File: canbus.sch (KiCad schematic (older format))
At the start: 14 parts, among them U6 ISO1050DUB

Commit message: Update according to comments
Also add missing connectors and update the fuses
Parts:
- removed FB?: GZ2012D601TF, symbol Device:Ferrite_Bead
- added C601: 10nF/50V, symbol Device:C
- added J602: Conn_02x02_Counter_Clockwise, symbol Connector_Generic:Conn_02x02_Counter_Clockwise
- added U601: RCLAMP0524P-N, symbol SH-ESP32:RCLAMP0524P-N
- F601: renamed from F?; value SMD1206P010TF -> FSMD012-1206-R; LCSC C20981 -> (none)
- gave numbers to parts that had none: 7
- renumbered C10 to C602, C9 to C604, JP1 to JP601, R11 to R601, U6 to U602
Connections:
- net labels added: Vin
- wire segments 46 -> 65
- no-connect marks 0 -> 4
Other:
- note added: "Optional termination\nresistance for the bus"
- note added: "This jumper can be bridged to\npower the whole device from\nCAN bus."
- moved on the sheet: F601, FB601, JP601, R601

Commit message: Rough PCB layout
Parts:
- removed J601: Screw_Terminal_01x05, symbol Connector:Screw_Terminal_01x05
- removed J602: Conn_02x02_Counter_Clockwise, symbol Connector_Generic:Conn_02x02_Counter_Clockwise
- added J601: Conn_01x04, Connector_Phoenix_MC:PhoenixContact_MCV_1,5_4-G-3.81_1x04_P3.81mm_Vertical, symbol Connector_Generic:Conn_01x04
- C601: footprint (none) -> Capacitor_SMD:C_0603_1608Metric
- C602, C604: footprint Capacitor_SMD:C_0603_1608Metric -> Capacitor_SMD:C_0402_1005Metric
- C603: footprint Capacitor_SMD:C_1206_3216Metric -> Capacitor_SMD:C_0805_2012Metric
- FB601: footprint (none) -> Inductor_SMD:L_0805_2012Metric
- U601: footprint (none) -> Package_DFN_QFN:Diodes_UDFN-10_1.0x2.5mm_P0.5mm
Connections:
- net labels added: +3.3V
- net labels removed: 3.3V, CAN_SHIELD, GNDPWR, Vin
- wire segments 65 -> 57
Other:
- note added: "NMEA 2000"
- note removed: "CAN bus"
- note removed: "This jumper can be bridged to\npower the whole device from\nCAN bus."
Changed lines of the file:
@@
 	6550 4000 6350 4000
-Wire Wire Line
-	6550 3150 6550 3350
 Wire Wire Line
 	6450 4300 6350 4300
@@
 F 0 "C604" H 6500 3650 50  0000 L CNN
 F 1 "100nF" H 6450 3550 50  0000 L CNN
-F 2 "Capacitor_SMD:C_0603_1608Metric" H 6838 3450 50  0001 C CNN
+F 2 "Capacitor_SMD:C_0402_1005Metric" H 6838 3450 50  0001 C CNN
 F 3 "~" H 6800 3600 50  0001 C CNN
 F 4 "C14663" H 6800 3600 50  0001 C CNN "LCSC"
@@
 Wire Wire Line
 	6800 3350 6550 3350
-Connection ~ 6550 3350
 Wire Wire Line
 	6550 3350 6550 4000
@@
 F 0 "C602" H 5015 4296 50  0000 L CNN
 F 1 "100nF" H 5015 4205 50  0000 L CNN
-F 2 "Capacitor_SMD:C_0603_1608Metric" H 4938 4100 50  0001 C CNN
+F 2 "Capacitor_SMD:C_0402_1005Metric" H 4938 4100 50  0001 C CNN
 F 3 "~" H 4900 4250 50  0001 C CNN
 F 4 "C14663" H 4900 4250 50  0001 C CNN "LCSC"
@@
 F 0 "FB601" V 4176 1450 50  0000 C CNN
 F 1 "GZ2012D601TF" V 4267 1450 50  0000 C CNN
-F 2 "" V 4380 1450 50  0001 C CNN
+F 2 "Inductor_SMD:L_0805_2012Metric" V 4380 1450 50  0001 C CNN
 F 3 "~" H 4450 1450 50  0001 C CNN
 F 4 "C1017" V 4450 1450 50  0001 C CNN "LCSC"
@@
 	0    -1   1    0
 $EndComp
-Text Notes 1550 2050 2    50   ~ 0
-CAN bus
+Text Notes 1400 2050 2    50   ~ 0
+NMEA 2000
 Text Label 3050 2200 0    50   ~ 0
 CAN_GND
@@
 Text Label 5550 4300 2    50   ~ 0
 CAN_GND
-Wire Wire Line
-	1850 2000 2000 2000
-Wire Wire Line
-	2000 2000 2000 1000
-Text Label 2000 1000 0    50   ~ 0
-CAN_SHIELD
-$Comp
-L power:GNDPWR #PWR0601
-U 1 1 5FA29442
-P 1650 1200
-F 0 "#PWR0601" H 1650 1000 50  0001 C CNN
-F 1 "GNDPWR" H 1654 1046 50  0000 C CNN
-F 2 "" H 1650 1150 50  0001 C CNN
-F 3 "" H 1650 1150 50  0001 C CNN
-	1    1650 1200
-	-1   0    0    -1
-$EndComp
-Wire Wire Line
-	1650 1200 1650 1000
-Wire Wire Line
-	1650 1000 2000 1000
 Wire Wire Line
 	4600 1450 4850 1450
@@
 F 0 "C603" H 6515 1846 50  0000 L CNN
 F 1 "2.2uF/50V" H 6515 1755 50  0000 L CNN
-F 2 "Capacitor_SMD:C_1206_3216Metric" H 6438 1650 50  0001 C CNN
+F 2 "Capacitor_SMD:C_0805_2012Metric" H 6438 1650 50  0001 C CNN
 F 3 "~" H 6400 1800 50  0001 C CNN
 F 4 "C50254" H 6400 1800 50  0001 C CNN "LCSC"
@@
 	1    0    0    -1
 $EndComp
-Text GLabel 6550 3150 1    50   Input ~ 0
-3.3V
-$Comp
-L Connector:Screw_Terminal_01x05 J601
-U 1 1 5FA210D6
-P 1650 2200
-F 0 "J601" H 1730 2242 50  0000 L CNN
-F 1 "Screw_Terminal_01x05" H 1730 2151 50  0000 L CNN
-F 2 "" H 1650 2200 50  0001 C CNN
-F 3 "~" H 1650 2200 50  0001 C CNN
-	1    1650 2200
-	-1   0    0    -1
-$EndComp
 Wire Wire Line
 	1850 2100 3050 2100
@@
 F 0 "U601" H 3300 3375 50  0000 C CNN
 F 1 "RCLAMP0524P-N" H 3300 3284 50  0000 C CNN
-F 2 "" H 3300 2850 50  0001 C CNN
+F 2 "Package_DFN_QFN:Diodes_UDFN-10_1.0x2.5mm_P0.5mm" H 3300 2850 50  0001 C CNN
 F 3 "" H 3300 2850 50  0001 C CNN
 	1    3300 2950
 	1    0    0    -1
 $EndComp
-Wire Wire Line
-	4100 2300 3750 2300
-Wire Wire Line
-	1850 2400 2800 2400
-Wire Wire Line
-	2950 2750 2900 2750
-Wire Wire Line
-	2900 2750 2900 2300
-Connection ~ 2900 2300
-Wire Wire Line
-	2900 2300 1850 2300
-Wire Wire Line
-	3650 2750 3750 2750
-Wire Wire Line
-	3750 2750 3750 2300
-Connection ~ 3750 2300
-Wire Wire Line
-	3750 2300 2900 2300
-Wire Wire Line
-	2950 2850 2800 2850
-Wire Wire Line
-	2800 2850 2800 2400
-Connection ~ 2800 2400
-Wire Wire Line
-	2800 2400 3850 2400
-Wire Wire Line
-	3650 2850 3850 2850
-Wire Wire Line
-	3850 2850 3850 2400
-Connection ~ 3850 2400
-Wire Wire Line
-	3850 2400 4100 2400
 NoConn ~ 2950 2950
 NoConn ~ 2950 3050
@@
 F 0 "C601" H 4965 1796 50  0000 L CNN
 F 1 "10nF/50V" H 4965 1705 50  0000 L CNN
-F 2 "" H 4888 1600 50  0001 C CNN
+F 2 "Capacitor_SMD:C_0603_1608Metric" H 4888 1600 50  0001 C CNN
 F 3 "~" H 4850 1750 50  0001 C CNN
 	1    4850 1750
@@
 Text Notes 1000 4950 0    50   ~ 0
 Optional termination\nresistance for the bus
-$Comp
-L Connector_Generic:Conn_02x02_Counter_Clockwise J602
-U 1 1 5F8C42B2
-P 2250 5750
-F 0 "J602" H 2300 5967 50  0000 C CNN
-F 1 "Conn_02x02_Counter_Clockwise" H 2300 5876 50  0000 C CNN
-F 2 "" H 2250 5750 50  0001 C CNN
-F 3 "~" H 2250 5750 50  0001 C CNN
-	1    2250 5750
-	1    0    0    -1
-$EndComp
-Text Label 2550 5850 0    50   ~ 0
-CAN_GND
-Text Label 2550 5750 0    50   ~ 0
-CAN_12V
 Wire Wire Line
 	3950 1450 4300 1450
 $Comp
-L power:GND #PWR0604
-U 1 1 5F8D1CCC
-P 1850 6050
-F 0 "#PWR0604" H 1850 5800 50  0001 C CNN
-F 1 "GND" H 1855 5877 50  0000 C CNN
-F 2 "" H 1850 6050 50  0001 C CNN
-F 3 "" H 1850 6050 50  0001 C CNN
-	1    1850 6050
-	1    0    0    -1
-$EndComp
-Wire Wire Line
-	1850 6050 1850 5850
-Wire Wire Line
-	1850 5850 2050 5850
-Text HLabel 1850 5750 0    50   Input ~ 0
-Vin
-Wire Wire Line
-	1850 5750 2050 5750
-Text Notes 2250 6300 0    50   ~ 0
-This jumper can be bridged to\npower the whole device from\nCAN bus.
+L power:+3.3V #PWR0103
+U 1 1 5F949C80
+P 6550 3350
+F 0 "#PWR0103" H 6550 3200 50  0001 C CNN
+F 1 "+3.3V" H 6565 3523 50  0000 C CNN
+F 2 "" H 6550 3350 50  0001 C CNN
+F 3 "" H 6550 3350 50  0001 C CNN
+	1    6550 3350
+	1    0    0    -1
+$EndComp
+Connection ~ 6550 3350
+$Comp
+L Connector_Generic:Conn_01x04 J601
+U 1 1 5F94CFA1
+P 1650 2200
+F 0 "J601" H 1568 2517 50  0000 C CNN
+F 1 "Conn_01x04" H 1568 2426 50  0000 C CNN
+F 2 "Connector_Phoenix_MC:PhoenixContact_MCV_1,5_4-G-3.81_1x04_P3.81mm_Vertical" H 1650 2200 50  0001 C CNN
+F 3 "~" H 1650 2200 50  0001 C CNN
+	1    1650 2200
+	-1   0    0    -1
+$EndComp
+Wire Wire Line
+	1850 2300 2800 2300
+Wire Wire Line
+	1850 2400 2900 2400
+Wire Wire Line
+	2950 2750 2900 2750
+Wire Wire Line
+	2900 2750 2900 2400
+Connection ~ 2900 2400
+Wire Wire Line
+	2900 2400 3700 2400
+Wire Wire Line
+	3650 2750 3700 2750
+Wire Wire Line
+	3700 2750 3700 2400
+Connection ~ 3700 2400
+Wire Wire Line
+	3700 2400 4100 2400
+Wire Wire Line
+	2950 2850 2800 2850
+Wire Wire Line
+	2800 2850 2800 2300
+Connection ~ 2800 2300
+Wire Wire Line
+	2800 2300 3800 2300
+Wire Wire Line
+	3650 2850 3800 2850
+Wire Wire Line
+	3800 2850 3800 2300
+Connection ~ 3800 2300
+Wire Wire Line
+	3800 2300 4100 2300
 $EndSCHEMATC

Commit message: Specified JLCPCB footprints for components
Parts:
- C601: footprint Capacitor_SMD:C_0603_1608Metric -> Capacitor_SMD:C_0402_1005Metric; LCSC (none) -> C15195
- C602, C604: LCSC C14663 -> C1525
- F601: LCSC (none) -> C220144
- J601: LCSC (none) -> C8410
- JP601: LCSC (none) -> C376075
- U601: LCSC (none) -> C316044
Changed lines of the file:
@@
 F 2 "Connector_PinHeader_2.54mm:PinHeader_1x02_P2.54mm_Vertical" H 2300 5000 50  0001 C CNN
 F 3 "~" H 2300 5000 50  0001 C CNN
+F 4 "C376075" H 2300 5000 50  0001 C CNN "LCSC"
 	1    2300 5000
 	-1   0    0    1
@@
 F 2 "Capacitor_SMD:C_0402_1005Metric" H 6838 3450 50  0001 C CNN
 F 3 "~" H 6800 3600 50  0001 C CNN
-F 4 "C14663" H 6800 3600 50  0001 C CNN "LCSC"
+F 4 "C1525" H 6800 3600 50  0001 C CNN "LCSC"
 	1    6800 3600
 	-1   0    0    -1
@@
 F 2 "Capacitor_SMD:C_0402_1005Metric" H 4938 4100 50  0001 C CNN
 F 3 "~" H 4900 4250 50  0001 C CNN
-F 4 "C14663" H 4900 4250 50  0001 C CNN "LCSC"
+F 4 "C1525" H 4900 4250 50  0001 C CNN "LCSC"
 	1    4900 4250
 	-1   0    0    -1
@@
 F 2 "Fuse:Fuse_1206_3216Metric" H 3850 1250 50  0001 L CNN
 F 3 "~" H 3800 1450 50  0001 C CNN
-F 4 "" H 3800 1450 50  0001 C CNN "LCSC"
+F 4 "C220144" H 3800 1450 50  0001 C CNN "LCSC"
 	1    3800 1450
 	0    1    1    0
@@
 F 2 "Package_DFN_QFN:Diodes_UDFN-10_1.0x2.5mm_P0.5mm" H 3300 2850 50  0001 C CNN
 F 3 "" H 3300 2850 50  0001 C CNN
+F 4 "C316044" H 3300 2950 50  0001 C CNN "LCSC"
 	1    3300 2950
 	1    0    0    -1
@@
 F 0 "C601" H 4965 1796 50  0000 L CNN
 F 1 "10nF/50V" H 4965 1705 50  0000 L CNN
-F 2 "Capacitor_SMD:C_0603_1608Metric" H 4888 1600 50  0001 C CNN
+F 2 "Capacitor_SMD:C_0402_1005Metric" H 4888 1600 50  0001 C CNN
 F 3 "~" H 4850 1750 50  0001 C CNN
+F 4 "C15195" H 4850 1750 50  0001 C CNN "LCSC"
 	1    4850 1750
 	1    0    0    -1
@@
 F 2 "Connector_Phoenix_MC:PhoenixContact_MCV_1,5_4-G-3.81_1x04_P3.81mm_Vertical" H 1650 2200 50  0001 C CNN
 F 3 "~" H 1650 2200 50  0001 C CNN
+F 4 "C8410" H 1650 2200 50  0001 C CNN "LCSC"
 	1    1650 2200
 	-1   0    0    -1

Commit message: Change optocoupler types, improve ground planes and a lot of other smaller fixes
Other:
- note added: "Input voltage up to 40V"
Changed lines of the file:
@@
 Wire Wire Line
 	3800 2300 4100 2300
+Text Notes 7250 1050 0    50   ~ 0
+Input voltage up to 40V
 $EndSCHEMATC

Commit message: Fix the library for HT75xx
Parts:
- U603: symbol sailor-hat:HT75xx-1-SOT23 -> SH-ESP32:HT75xx-1-SOT23
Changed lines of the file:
@@
 $EndComp
 $Comp
-L sailor-hat:HT75xx-1-SOT23 U?
+L SH-ESP32:HT75xx-1-SOT23 U?
 U 1 1 5F94C95C
 P 7000 1550

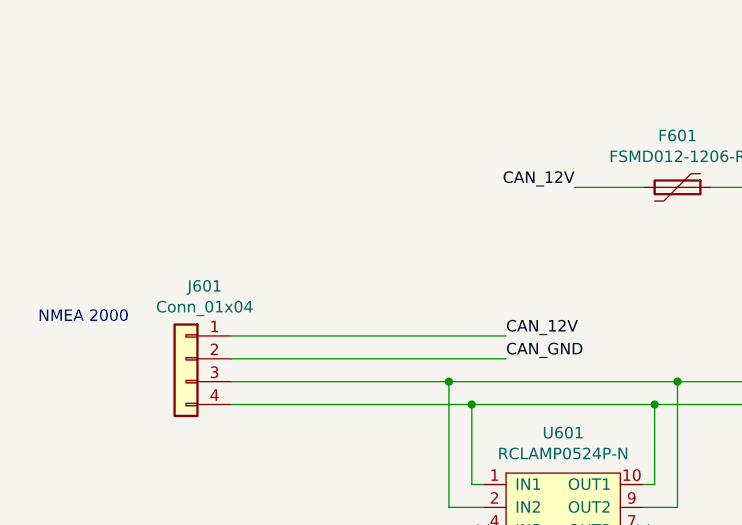
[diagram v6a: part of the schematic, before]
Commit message: WireLink from VCAN to VIN + protection diode.
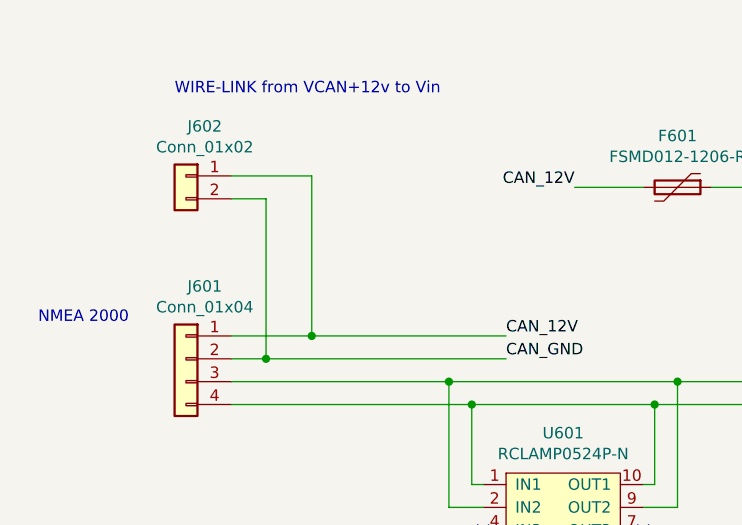
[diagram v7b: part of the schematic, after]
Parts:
- added J602: Conn_01x02, SH-ESP32:WireLink_1x02_P2.54mm, symbol Connector_Generic:Conn_01x02
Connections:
- net CAN_12V: now also J602.1 (Pin_1)
- net CAN_GND: now also J602.2 (Pin_2)
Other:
- note added: "WIRE-LINK from VCAN+12v to Vin"
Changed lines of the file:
@@
 $EndComp
 Wire Wire Line
-	1850 2100 3050 2100
+	1850 2100 2200 2100
 $Comp
 L SH-ESP32:RCLAMP0524P-N U601
@@
 	4850 1450 5400 1450
 Wire Wire Line
-	1850 2200 3050 2200
+	1850 2200 2000 2200
 Text Notes 1000 4950 0    50   ~ 0
 Optional termination\nresistance for the bus
@@
 Text Notes 7250 1050 0    50   ~ 0
 Input voltage up to 40V
+$Comp
+L Connector_Generic:Conn_01x02 J?
+U 1 1 5FB62718
+P 1650 1400
+AR Path="/5F6FAF6E/5FB62718" Ref="J?"  Part="1"
+AR Path="/5F733BA4/5FB62718" Ref="J602"  Part="1"
+F 0 "J602" H 1568 1617 50  0000 C CNN
+F 1 "Conn_01x02" H 1568 1526 50  0000 C CNN
+F 2 "SH-ESP32:WireLink_1x02_P2.54mm" H 1650 1400 50  0001 C CNN
+F 3 "~" H 1650 1400 50  0001 C CNN
+	1    1650 1400
+	-1   0    0    -1
+$EndComp
+Wire Wire Line
+	1850 1500 2000 1500
+Text Notes 1600 1050 0    50   ~ 0
+WIRE-LINK from VCAN+12v to Vin
+Wire Wire Line
+	1850 1400 2200 1400
+Wire Wire Line
+	2200 1400 2200 2100
+Connection ~ 2200 2100
+Wire Wire Line
+	2200 2100 3050 2100
+Wire Wire Line
+	2000 1500 2000 2200
+Connection ~ 2000 2200
+Wire Wire Line
+	2000 2200 3050 2200
 $EndSCHEMATC
